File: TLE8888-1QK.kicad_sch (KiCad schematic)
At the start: 40 parts, among them J15 Conn_01x01, J17 Conn_01x01, Q1 IPD30N06S2L-23, U2 TLE8888QK

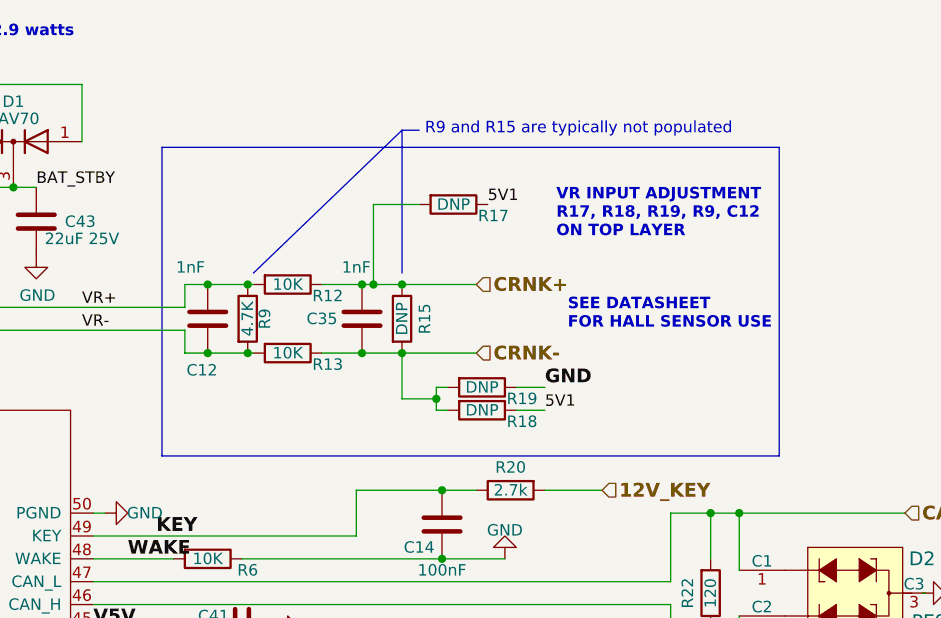
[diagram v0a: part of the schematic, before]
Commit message: replaces micro b connector by usb-c
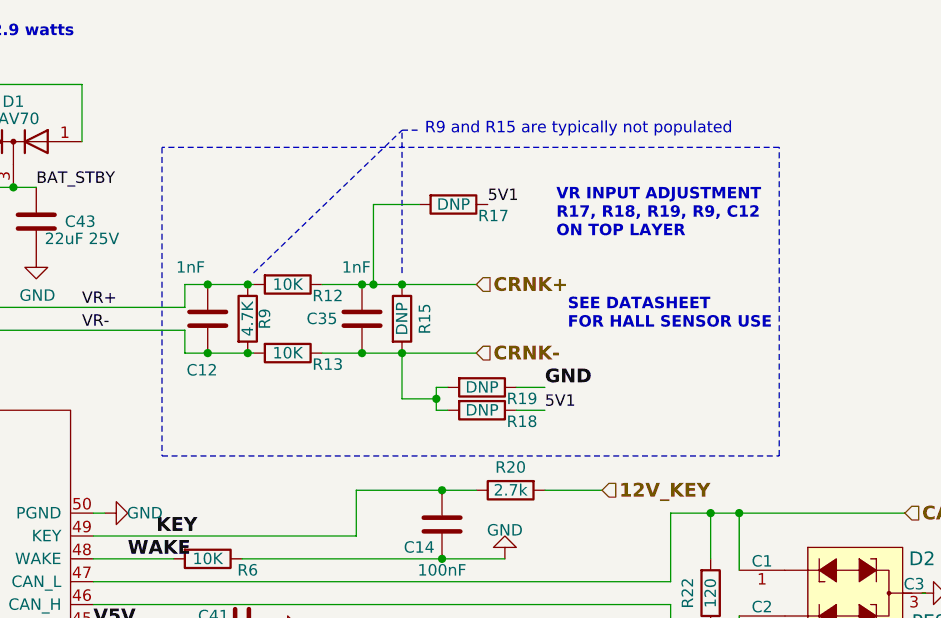
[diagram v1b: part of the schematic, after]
